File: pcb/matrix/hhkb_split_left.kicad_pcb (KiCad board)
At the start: 2 copper layers, 140.4 x 97.4 mm, 65 parts, among them SW1 CPG151101S11-2, SW10 CPG151101S11-2, SW11 CPG151101S11-2, SW12 CPG151101S11-2, SW13 CPG151101S11-2, SW14 CPG151101S11-2, SW15 CPG151101S11-2, SW16 CPG151101S11-2, SW17 CPG151101S11-2, SW18 CPG151101S11-2, SW19 CPG151101S11-2, SW2 CPG151101S11-2, SW20 CPG151101S11-2, SW21 CPG151101S11-2, SW22 CPG151101S11-2, SW23 CPG151101S11-2, SW24 CPG151101S11-2, SW25 CPG151101S11-2, SW26 CPG151101S11-2, SW27 CPG151101S11-2, SW3 CPG151101S11-2, SW4 CPG151101S11-2, SW5 CPG151101S11-2, SW6 CPG151101S11-2, SW7 CPG151101S11-2, SW8 CPG151101S11-2, SW9 CPG151101S11-2, U1 74LVC595

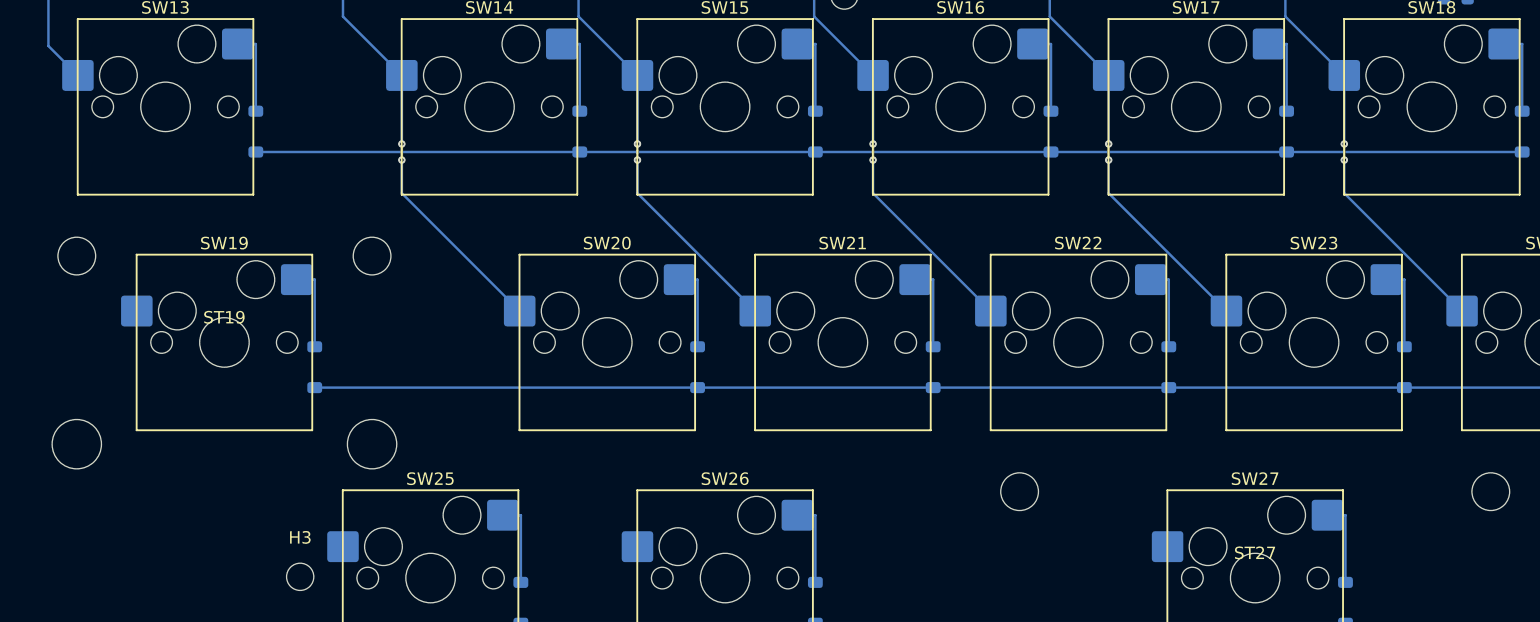
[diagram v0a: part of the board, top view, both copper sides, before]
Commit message: 左のキーマトリクスを完成させた（21 ホップ全部・DRC 0）
引けなかった 4 本を潰した。**どれも基板の都合ではなく、引き方が
硬かっただけ**だった（残っていた「障害物」は 4 本中 1 本も無い）。

足した形:
  C  跨いだあと、行の下で 45° に寄る
  C' 横が縦より長いとき、行の下を横に走ってから 45° で降りる
  D  跨いだ直後にレーンで横へ逃げてから降りる

踏んだ穴を注記に残した:
  - `knee < 0` を手前で弾いていて、そのために書いた C' が**一度も
    呼ばれていなかった**（左 COL3/COL5）
  - 行のバスは線ではなく**パッドの列**でもある。線だけ避けて K 側
    パッド（半対角 0.75mm）を 0.65mm で擦っていた（左 COL1/3/5）
  - 全列を同じ y のレーンに流して**自分どうしで交差**した
    （COL1/COL3/COL5 が y=124.000 に重なり tracks_crossing 2 件）。
    自分の障害物だけ見て、自分どうしを見ていなかった → 列ごとに
    レーンをずらす（LANE_PITCH）
  - C は縦の区間が元の x に長く残るので、スタビの穴（ST19 が列の
    x のほぼ真上）を抜けられなかった → D で先に横へ逃げる

左: 行 22 / 列 88 区間 / 橋のビア 42 個 / 引かなかったホップ 0。
配線由来の DRC 違反 0。残る未接続 17 件は全部 U1 / J_DB / C_U1 で、
キーとダイオードの間の未接続は 0（利用者の指示どおり MCU は無視）。

右は 6 ホップ残っている（別途）。

Co-Authored-By: Claude Opus 5 (1M context) <noreply@anthropic.com>
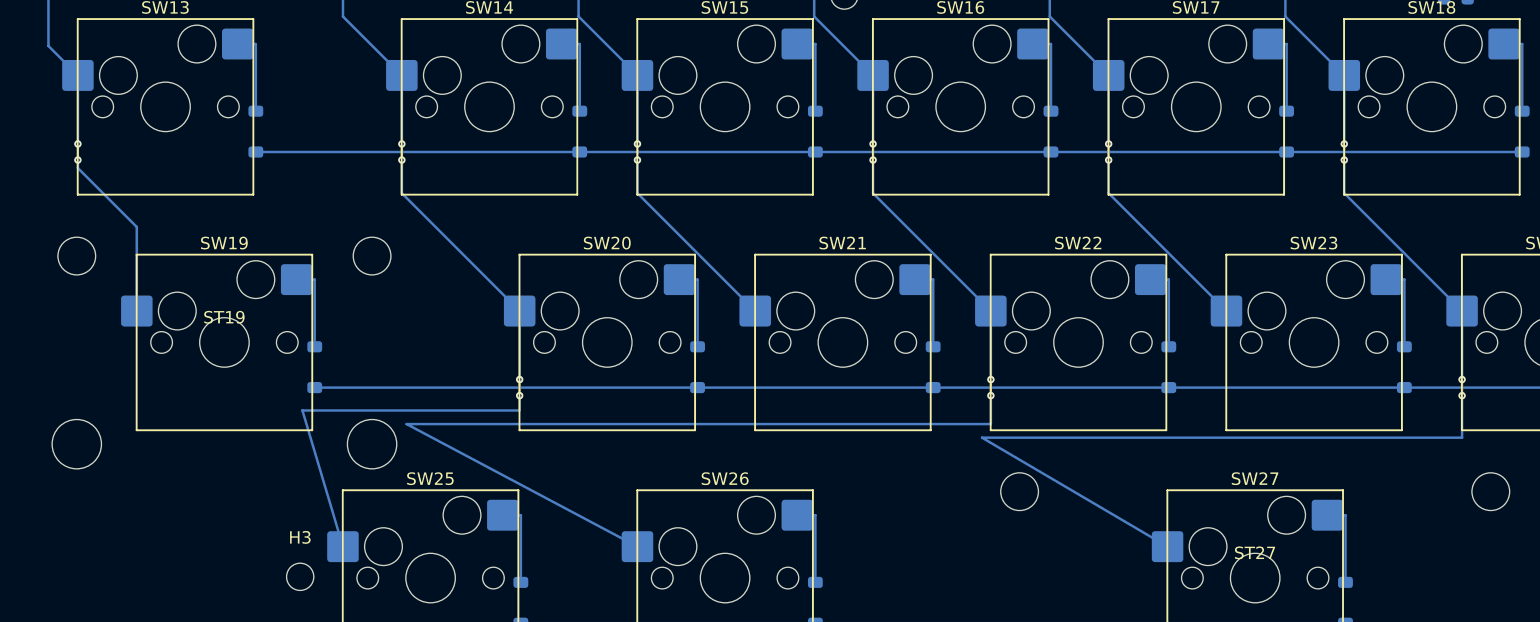
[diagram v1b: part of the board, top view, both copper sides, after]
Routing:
- net COL3: track 67.0 -> 144.5 mm, vias 6 -> 8
- net COL5: track 67.0 -> 133.5 mm, vias 6 -> 8
- net COL1: track 67.0 -> 104.1 mm, vias 6 -> 8
- net COL0: track 41.1 -> 62.1 mm, vias 4 -> 6

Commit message: 最下段の列の配線を短くした（横断 164.44 → 89.79mm）
利用者の指摘「一番下の行だけ変ですね。そもそもそのキーがその列番号に
あることが妥当なのか、と言うところから疑って」。

**疑ったら、割り当ての方が間違っていた。**最下段は幅広キー
（Alt / Meta 1.5u / L-Space 3.0u）で、dtsi が **キーの真上を通らない列**
を選んでいる。実測: Meta は範囲 47.6〜76.2 に COL1/COL2 が通っている
のに COL3(90.5) を指定。L-Space は COL4 なら 4.76mm のところ COL5 で
14.29mm。**配線が長い横断になるのは当然だった。**

⚠️ **私は当初「割り当ては妥当」と報告したが誤りだった。**コードと
dtsi の一致しか見ておらず、**dtsi 自体（自分たちの生成物）が妥当かを
見ていなかった。**「自分の生成物どうしの一致は検証ではない」。

**ファームの修正は open-gaps #46 に記録した**（利用者「後でもできるので、
とりあえず配線を」）。ここでは配線側だけ短くする。

足した形と直した穴:
  E   下のキーの x で降ろし、横移動は行の上でやる（COL1 が採用）
  C'  **符号が逆で、目標を追い越してから戻っていた**（COL3 は
      x=117.1 まで行って 135.8 へ戻り、18.7mm 無駄にしていた）
  候補は**短い順に試す**。定義順だと先に書いた形が勝って長い経路が残る

左: 21 ホップ全部・列 88 区間・橋のビア 42 個・配線由来の DRC 違反 0。
未接続 17 件は全部 U1 / J_DB / C_U1（指示どおり MCU は無視）。
右は 4 ホップ残り（別途）。

Co-Authored-By: Claude Opus 5 (1M context) <noreply@anthropic.com>
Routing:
- net COL3: track 144.5 -> 108.8 mm
- net COL5: track 133.5 -> 104.7 mm
- net COL1: track 104.1 -> 93.9 mm

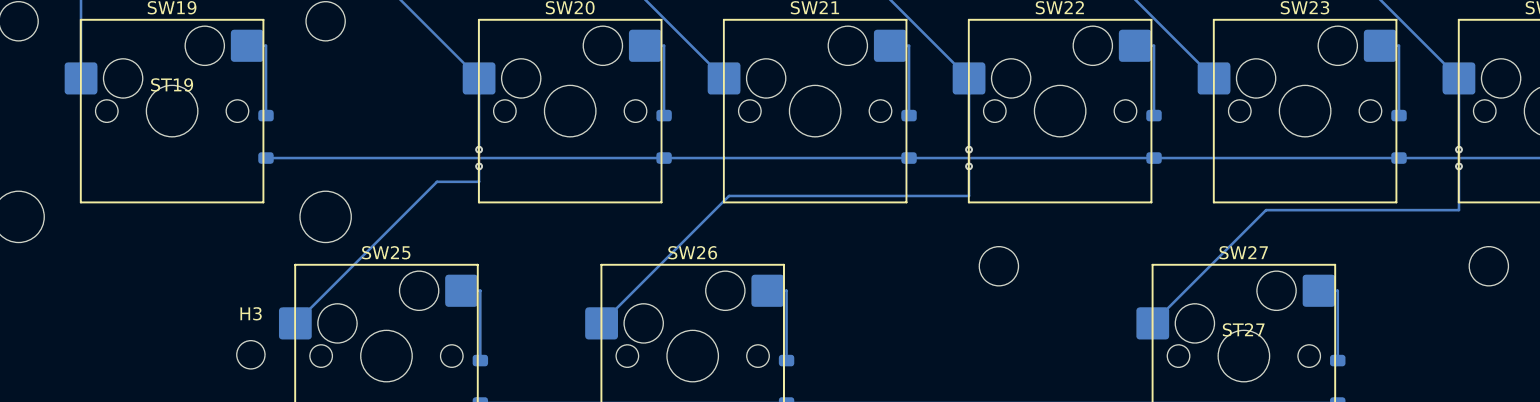
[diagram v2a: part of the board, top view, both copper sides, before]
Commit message: 最下段を列 0/1/3 に繋いだ（利用者の指定）
利用者「答えを言います。SW25: COL0 / SW26: COL1 / SW27: COL3」。

**私の案（COL1/COL2/COL4）より良い。**中心との距離だけで選んでいて、
「一番左のキーに一番左の列」という並びの素直さを見ていなかった:

  Alt      範囲  28.58〜 47.62   COL0 x= 21.43（外れる 16.67mm）
  Meta     範囲  47.62〜 76.20   COL1 x= 52.39 … **キーの真上**
  L-Space  範囲  76.20〜133.35   COL3 x= 90.49 … **キーの真上**

3 本中 2 本がキーの真上を通る。最下段の配線は
**164.44 → 89.79 → 62.85mm**（元の 38%）。左は 21 ホップ全部・
配線由来の DRC 違反 0 のまま。

⚠️ **前回「SW26 が COL3 であるべきではない」と書いておきながら、
割り当てを直さず配線だけ短くしていた。**利用者「COL3 につながって
ますけど？」で発覚。**言ったことと、やったことが違っていた。**

ついでに検査の穴を 1 つ塞いだ:
  `check_zmk_config.count_map_entries` が**コメントを落とさずに
  `RC(` を数えていた。**map の中に経緯を書いてそこに旧値を引用したら
  +3 に数えて「バインディングが 3 個足りない」と嘘の赤を出した。
  同じファイルを読む `implied_positions` は最初からコメントを
  落としており、**2 つの関数で扱いが違っていた**。
  故意に壊して確かめた（コメント内の RC( では落ちず、本物の増減では
  落ちる）。

open-gaps #46 は左については解決。**右の最下段は未測定のまま残る。**

Co-Authored-By: Claude Opus 5 (1M context) <noreply@anthropic.com>
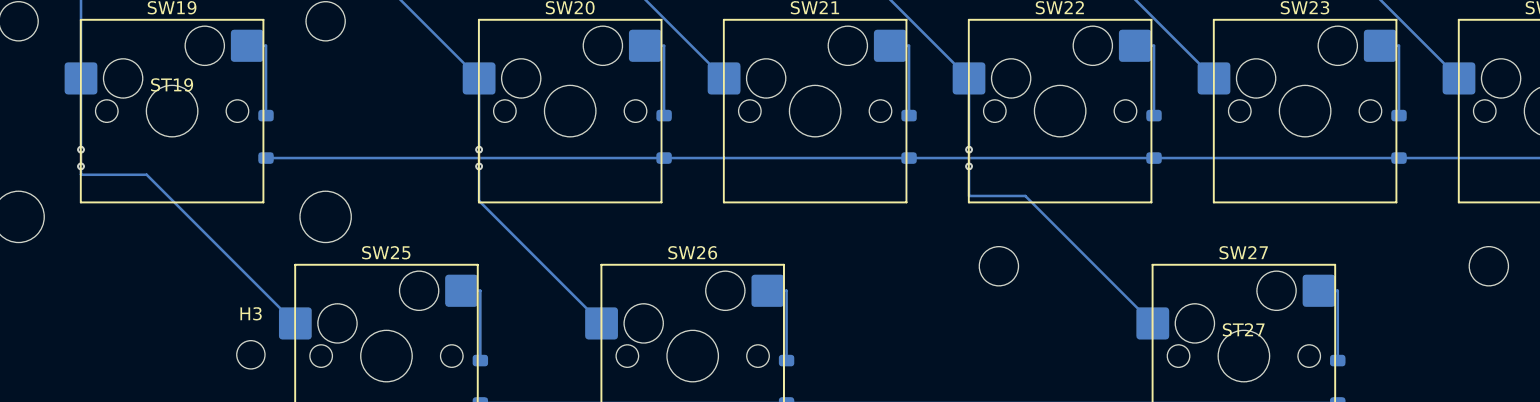
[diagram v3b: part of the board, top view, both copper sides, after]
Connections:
- SW25 pad 1: COL1 -> COL0
- SW26 pad 1: COL3 -> COL1
- SW27 pad 1: COL5 -> COL3
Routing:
- net COL5: track 104.7 -> 67.0 mm, vias 8 -> 6
- net COL0: track 62.1 -> 91.0 mm, vias 6 -> 8
- net COL3: track 108.8 -> 94.5 mm
- net COL1: track 93.9 -> 90.0 mm

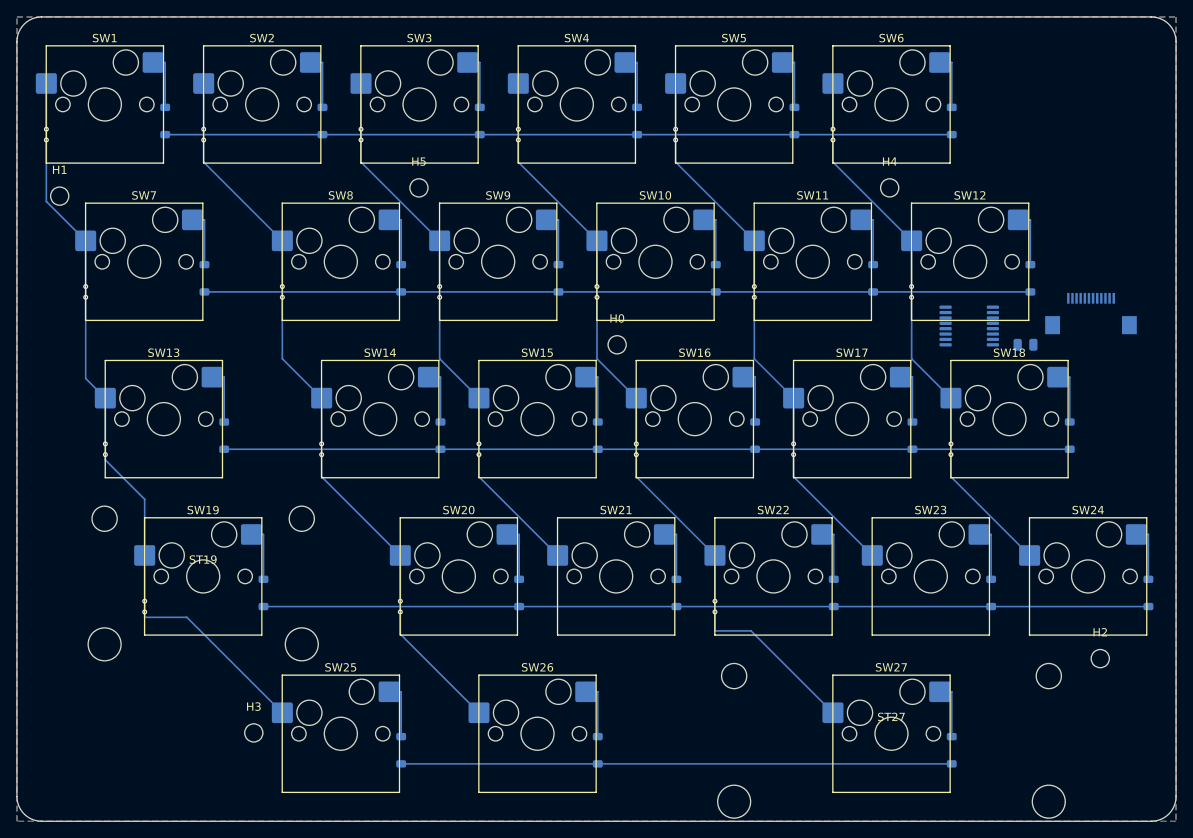
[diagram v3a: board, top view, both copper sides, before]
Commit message: COL0 を裏だけで引いた（行は無限に長い線ではない）
利用者「COL0 は全て B.Cu 側でよく、F.Cu 側にビアでもぐる必要はない
はずです」。**そのとおりだった。**

**私の検査は行を「その y の無限に長い線」として見ていた。**実際には
行のバスには x の範囲がある。測ると **COL0 は一番左の列で、どの行も
COL0 より右から始まっていた**:

    ROW_C  y=65.55   x  97.769〜193.019   COL0 は x=83.384 ← 左に外れる
    ROW_E  y=84.60   x 102.531〜202.544   COL0 は x=88.146 ← 外れる
    ROW_D  y=103.65  x 104.912〜207.306   COL0 は x=90.528 ← 外れる

**跨いでいない行のために橋を 3 つ架けていた。**row_span で x の範囲も
持ち、その x に行が実在するときだけ「跨ぐ」と数えるようにした。
跨ぐ行が無いホップは裏だけで引く（ビア 0）。

残る 1 つ（SW19→SW25）は**本物**。行き先の SW25 が x=111.959 で、
ROW_B の範囲（109.675〜216.831）の中に入るため。

ついでに、跨がないホップ用に「縦 → 45° → 縦」で寄る高さを選べる形を
足した。SW13→SW19 は ST19 の穴（x=90.437 が列の x=90.528 の真上）で
素直な 2 つの形が両方詰むが、寄る高さを振れば抜けられる。

左: 21 ホップ全部・列 81 区間・橋のビア 42→36 個・配線由来の DRC 違反 0。
右は COL0 が元から行の左に居るため変化なし（no-op と確認して戻した）。

Co-Authored-By: Claude Opus 5 (1M context) <noreply@anthropic.com>
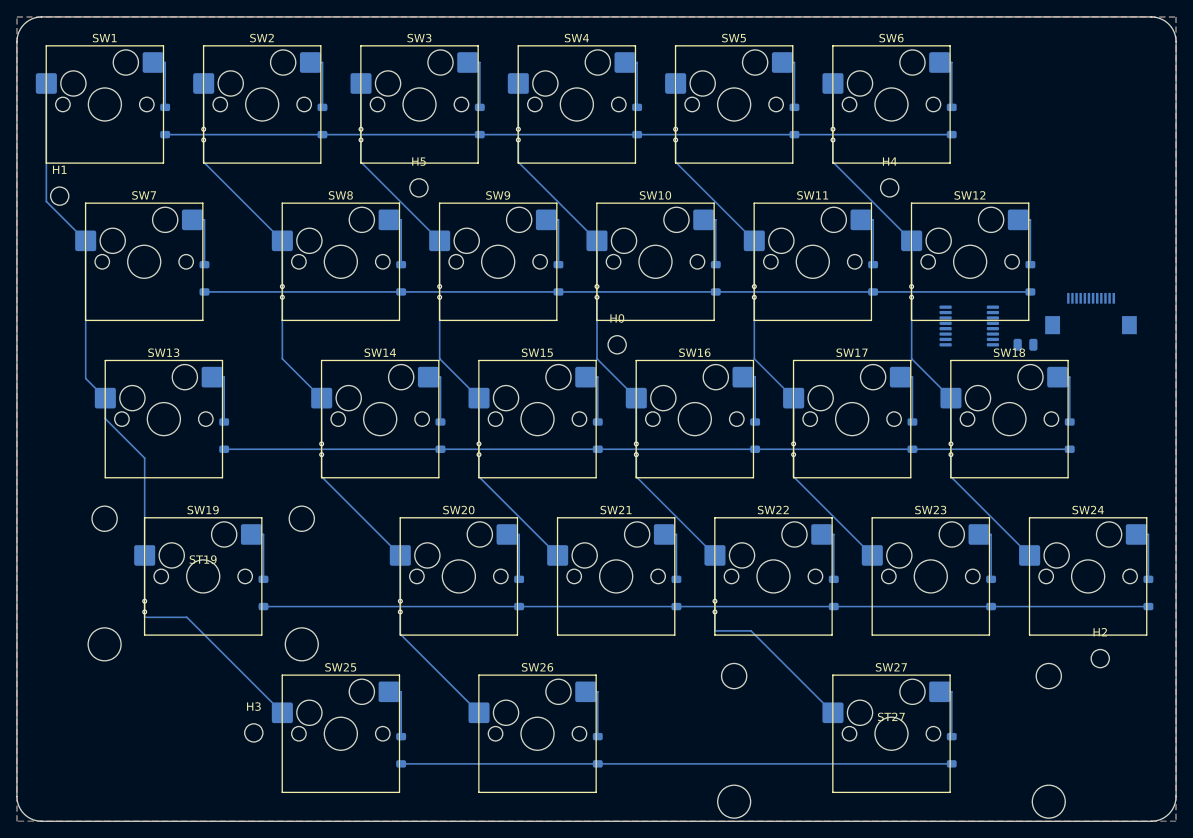
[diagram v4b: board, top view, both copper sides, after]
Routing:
- net COL0: vias 8 -> 2

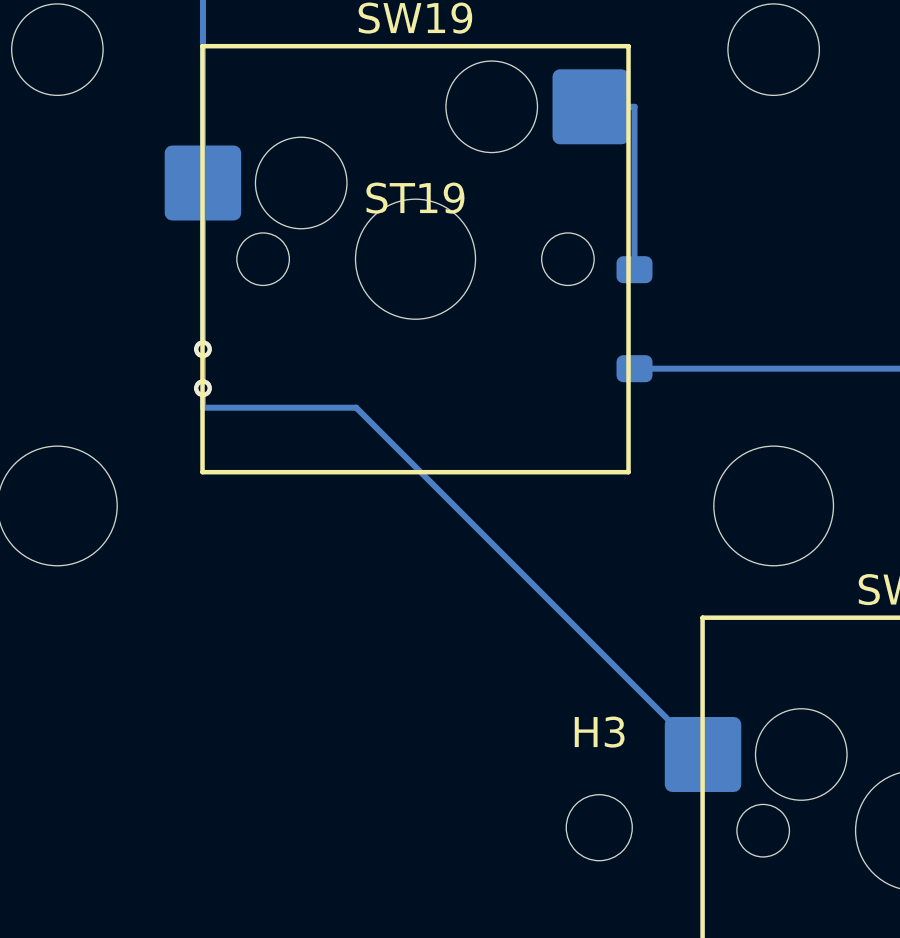
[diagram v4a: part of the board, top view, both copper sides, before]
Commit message: COL0 のビアを 0 にした（跨ぐ点の x で見る）
利用者「どう見てもいらないんだけど」。**そのとおりだった。**

前回 row_span（行の x の範囲）を入れたのに、判定を
`_row_blocks(ry, ax) or _row_blocks(ry, cx)` と書いていた。
**行き先の x に行があるだけで橋を架けていた。**COL0 の SW19→SW25 は
x=95.290 で y=122.7 を通るのに、ROW_B は x=109.675 からで 14.4mm 右。
**そこに行は無い。**横へ寄るのは行を過ぎたあとなので cx は関係ない。

さらに斜めの区間では、**交わる点の x は端点のどちらとも違う**。
この経路は 45° の途中 x=99.099 で y=122.7 を通る（やはり ROW_B の
左端より左）。端点で見ていたので、引けるはずのホップを弾いていた。

**跨ぐ点の x を内挿して見る**ようにした。これで COL0 は
**ビア 0 個・F.Cu 0 本**の一本道になった（前回 2 個 → 0 個）。
左全体の橋も 36 → 34 個。21 ホップ全部・配線由来の DRC 違反 0。

右は COL0 が元から行の左に居るため変化なし（no-op と確認して戻した）。

Co-Authored-By: Claude Opus 5 (1M context) <noreply@anthropic.com>
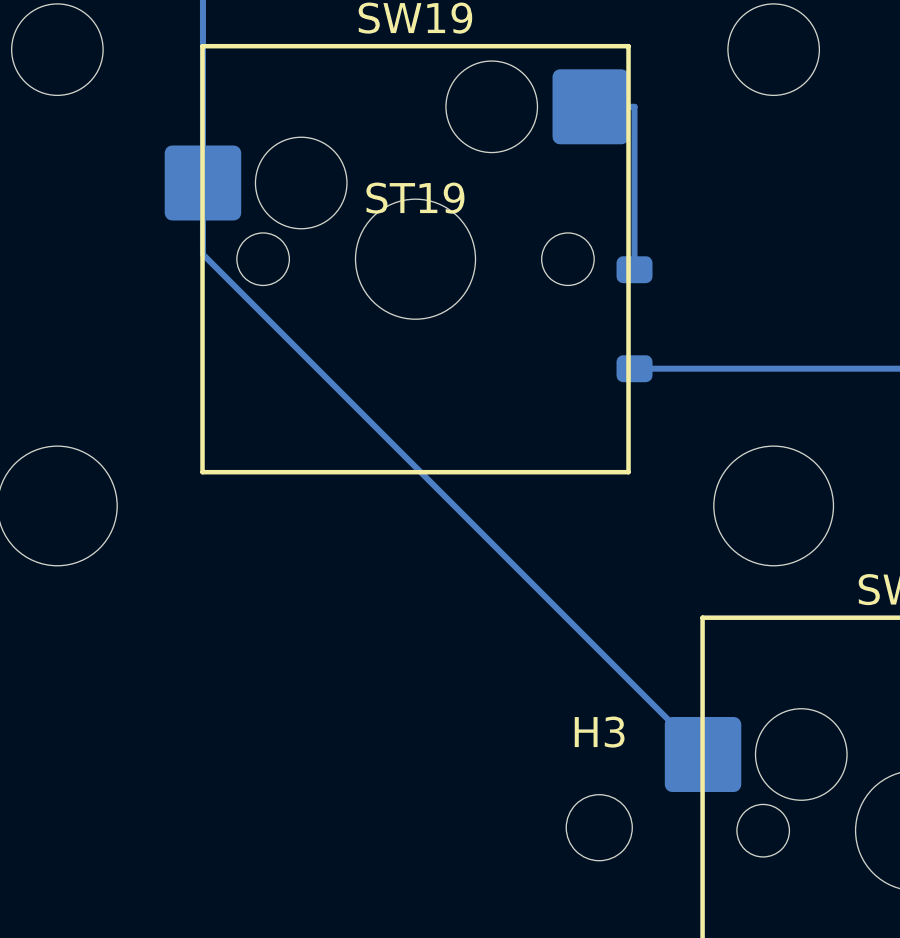
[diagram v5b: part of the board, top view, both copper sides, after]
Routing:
- net COL0: track 91.0 -> 88.0 mm, vias 2 -> 0

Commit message: 穴とのギリギリを解消した（0.330 → 1.030mm）
利用者「SW19、配線が穴にかなりギリギリです」→「画像ちゃんと見た？
他にも方法あるだろ」。**両方そのとおりだった。**

**私は探し方を自分で狭めていた。**パッドから右下へ 45° で出る形だけを
振って「0.33mm が上限」と報告した。中継点を 1 個自由に置いて探すと
**1.650mm** 空く経路があり、絵に写っていた左側の空き地を通っていた。
**画像を見れば分かることを、狭い総当りの結果で否定していた。**

45° 限定でも「**縦に降りてから曲がる**」形なら 1.030mm 取れる。
SW19 自身の胴（φ1.75 の位置決めポスト）を過ぎるまで真下に降りれば、
角をかすめずに済む。

2 つ直した:
  - 形の候補に「縦 → 45° → 横 → 縦」を足した
  - **候補は「最初に通ったもの」ではなく「一番余裕のあるもの」を採る**
    （_margin）。規格 0.25mm ぎりぎりの経路と 1.0mm 空く経路が
    どちらも「合格」になっていた

板全体で一番きつい箇所: **0.330 → 1.030mm**。COL0 が他の全列と同じ
値に揃った（他は元から 1.030mm）。COL0 のビアは 0 個のまま。
21 ホップ全部・配線由来の DRC 違反 0。

Co-Authored-By: Claude Opus 5 (1M context) <noreply@anthropic.com>
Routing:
- net COL0: track 88.0 -> 93.1 mm

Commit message: 右のマトリクスを完成させた（U1/U2 の移動を取り込み・引き残し 0）
利用者が基板上で U2 と U1 を動かした:
  「SW6 から SW15 は U2 をずらしたので、それで試してください」
  「SW16-24 は工夫して」
  「SW5, 6 だけど、他の同じ行の配線パターンを踏襲して」
  「コンデンサとか避けておいたので」

**U1/U2 の移動を生成器へ取り込んだ**（座標が完全一致することを確認）:
  U2  帯0 x=+15.0    → 帯1 x=-40.662 dy=+0.725  (109.338, 88.900)
  U1  帯0 x=+2.0     → 帯3 x=-75.938 dy=-0.025  ( 74.062,126.250)

どちらも**列の通り道を塞いでいた**。U2 は COL5（SW6→SW15）を、
U1 と C_U1 は COL4（x≈146〜152）を。移動で両方とも素直に降りられる。

**SW5 が同じ段の他と揃った**（利用者の指摘）。SW4/SW5/SW6 が
「0.200mm 降りて曲がり、75.650 で 45° を終える」と完全に同じ形。
前は SW5 だけ 3.700mm 降りていた（U1/C_U1 を避けるため）。

**SW16→SW24（ST24 のスタビ穴）は形 F で解いた。**C も D も曲がる y が
1 点に決まっており、そこが穴の真横だと 0.289mm しか空かない。
**曲がる高さを振れる形**を足すと、45° を保ったまま穴の左を抜けて
1.030mm 取れる（他の列と同じ値）。

2 つ直した:
  - 橋を架ける枝でも**余裕が最大の候補を採る**（他の枝は済んでいた）
  - `gen_matrix` が **GND の離島を繋いでいなかった**。配線が密になって
    ベタが割れ、DRC が「ゾーンが繋がっていない」を 2 件出した。
    本番と同じ `gnd_fanout.stitch_islands` を呼ぶ（左 10 個・右 12 個）。
    浮いた銅は 2.4GHz でアンテナになる

左右とも: **引かなかったホップ 0 / 配線由来の DRC 違反 0 /
マトリクス内の未接続 0 / 最小の隙間 1.030mm**。

⚠️ **C_U1 は取り込んでいない。**利用者の板では U1 から 136mm 離れており、
パスコンとして効かない位置（効くのは往復ループのインダクタンス）。
`DECOUPLE_BESIDE` が U1 から算出する仕組みのまま残した。

pytest の赤 8 件は**私の変更の前後で同じ**（本番 pcb/ が未再生成＝
open-gaps #47、SPARE 系は以前から）。

Co-Authored-By: Claude Opus 5 (1M context) <noreply@anthropic.com>
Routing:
- net COL5: track 67.0 -> 71.2 mm
- net COL2: track 67.0 -> 70.7 mm
- net GND: vias 0 -> 10
